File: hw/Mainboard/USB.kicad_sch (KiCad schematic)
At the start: 10 parts, among them J14 USB2.0_HOST_TYPE_C, J8 BOOTSEL

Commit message: wip
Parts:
- removed J8: BOOTSEL, Connector_PinHeader_2.54mm:PinHeader_1x04_P2.54mm_Vertical, symbol Connector:Conn_01x04_Male
- removed R73, R74: 5k1, Resistor_SMD:R_0402_1005Metric, symbol Device:R_Small
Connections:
- net +5V: now also PT19.1, PT20.1
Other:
- note added: "USB 2.0 Host over USB-C connector The 56k pullups on CC1 and CC2 identify as a downstream facing port supplying up to 900ma @ 5V."
- note removed: "USB 2.0 Host over USB-C connector As a host, the 56k pullups on CC1 and CC2 identify USB-C as a power source supplying up to 900ma @ 5V. When flashing the MCU, the 5.1k pulldowns on CC1 and CC2 identify USB-C as a power consumer."
- moved on the sheet: R35, R36

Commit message: hw: routing / silk wip
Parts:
- added C84: 10u, Capacitor_SMD:C_0603_1608Metric, symbol Device:C_Small
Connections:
- net +5V: now also C84.1
- net PD_GND: now also C84.2
- net VBUS1: now reaches J14.A4_B9 (VBUS), PT19.2, R35.1
- net VBUS2: now reaches J14.A9_B4 (VBUS), PT20.2, R36.1
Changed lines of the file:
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@@
   (junction (at 122.555 77.47) (diameter 0) (color 0 0 0 0)
+  )
+  (junction (at 102.87 77.47) (diameter 0) (color 0 0 0 0)
   )
   (no_connect (at 137.16 105.41))
   (no_connect (at 137.16 107.95))
   (wire (pts (xy 137.16 95.25) (xy 135.89 95.25))
+    (stroke (width 0) (type default) (color 0 0 0 0))
+  )
+  (wire (pts (xy 102.87 86.36) (xy 102.87 88.9))
     (stroke (width 0) (type default) (color 0 0 0 0))
   )
@@
     (stroke (width 0) (type default) (color 0 0 0 0))
   )
+  (wire (pts (xy 102.87 77.47) (xy 102.87 81.28))
+    (stroke (width 0) (type default) (color 0 0 0 0))
+  )
   (wire (pts (xy 125.73 85.09) (xy 122.555 85.09))
     (stroke (width 0) (type default) (color 0 0 0 0))
@@
     (effects (font (size 1.27 1.27)) (justify left bottom))
   )
+  (label "VBUS2" (at 129.54 77.47 0)
+    (effects (font (size 1.27 1.27)) (justify left bottom))
+  )
   (label "CC2" (at 137.16 85.09 180)
     (effects (font (size 1.27 1.27)) (justify right bottom))
+  )
+  (label "VBUS1" (at 129.54 74.93 0)
+    (effects (font (size 1.27 1.27)) (justify left bottom))
   )
   (label "CC1" (at 137.16 82.55 180)
@@
     (effects (font (size 1.27 1.27)) (justify right))
   )
+  (symbol (lib_id "Device:C_Small") (at 102.87 83.82 0) (unit 1)
+    (in_bom yes) (on_board yes)
+    (property "Reference" "C84" (id 0) (at 105.2068 82.6516 0)
+      (effects (font (size 1.27 1.27)) (justify left))
+    )
+    (property "Value" "10u" (id 1) (at 105.2068 84.963 0)
+      (effects (font (size 1.27 1.27)) (justify left))
+    )
+    (property "Footprint" "Capacitor_SMD:C_0603_1608Metric" (id 2) (at 102.87 83.82 0)
+      (effects (font (size 1.27 1.27)) hide)
+    )
+    (property "Datasheet" "https://datasheet.lcsc.com/lcsc/2304140030_Samsung-Electro-Mechanics-CL10A106MA8NRNC_C96446.pdf" (id 3) (at 102.87 83.82 0)
+      (effects (font (size 1.27 1.27)) hide)
+    )
+    (property "LCSC" "C96446" (id 4) (at 102.87 83.82 0)
+      (effects (font (size 1.27 1.27)) hide)
+    )
+    (pin "1")
+    (pin "2")
+  )
+  (symbol (lib_id "PET:PD_GND") (at 102.87 88.9 0) (unit 1)
+    (in_bom yes) (on_board yes) (fields_autoplaced)
+    (property "Reference" "#PWR0206" (id 0) (at 102.87 95.25 0)
+      (effects (font (size 1.27 1.27)) hide)
+    )
+    (property "Value" "PD_GND" (id 1) (at 102.87 93.98 0))
+    (property "Footprint" "" (id 2) (at 102.87 88.9 0)
+      (effects (font (size 1.27 1.27)) hide)
+    )
+    (property "Datasheet" "" (id 3) (at 102.87 88.9 0)
+      (effects (font (size 1.27 1.27)) hide)
+    )
+    (pin "1")
+  )
   (symbol (lib_id "PET:PowerTie_2") (at 113.03 74.93 0) (unit 1)

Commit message: hw: unstitched copper fills
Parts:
- C84: value 10u -> 4.7u 16V; LCSC C96446 -> C19666
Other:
- note added: "USB 2.0 Host over USB-C connector The 56k pullups on CC1 and CC2 identify as a downstream facing port supplying 5V @ 900ma."
- note removed: "USB 2.0 Host over USB-C connector The 56k pullups on CC1 and CC2 identify as a downstream facing port supplying up to 900ma @ 5V."
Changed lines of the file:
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@@
     (stroke (width 0) (type default) (color 0 0 0 0))
   )
-  (text "USB 2.0 Host over USB-C connector\n\nThe 56k pullups on CC1 and CC2 identify as a downstream\nfacing port supplying up to 900ma @ 5V."
-    (at 80.01 123.19 0)
+  (text "USB 2.0 Host over USB-C connector\n\nThe 56k pullups on CC1 and CC2 identify as a\ndownstream facing port supplying 5V @ 900ma."
+    (at 83.82 114.3 0)
     (effects (font (size 1.27 1.27)) (justify left bottom))
   )
@@
       (effects (font (size 1.27 1.27)) (justify left))
     )
-    (property "Value" "10u" (id 1) (at 105.2068 84.963 0)
+    (property "Value" "4.7u 16V" (id 1) (at 105.2068 84.963 0)
       (effects (font (size 1.27 1.27)) (justify left))
     )
@@
       (effects (font (size 1.27 1.27)) hide)
     )
-    (property "Datasheet" "https://datasheet.lcsc.com/lcsc/2304140030_Samsung-Electro-Mechanics-CL10A106MA8NRNC_C96446.pdf" (id 3) (at 102.87 83.82 0)
+    (property "Datasheet" "" (id 3) (at 102.87 83.82 0)
       (effects (font (size 1.27 1.27)) hide)
     )
-    (property "LCSC" "C96446" (id 4) (at 102.87 83.82 0)
+    (property "LCSC" "C19666" (id 4) (at 102.87 83.82 0)
       (effects (font (size 1.27 1.27)) hide)
     )

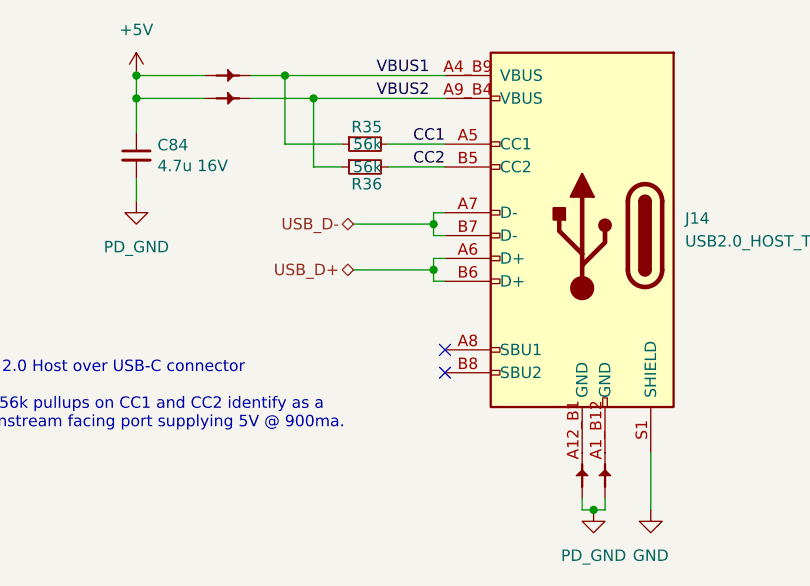
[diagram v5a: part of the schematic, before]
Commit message: hw: heat sink, trace size, more stitching
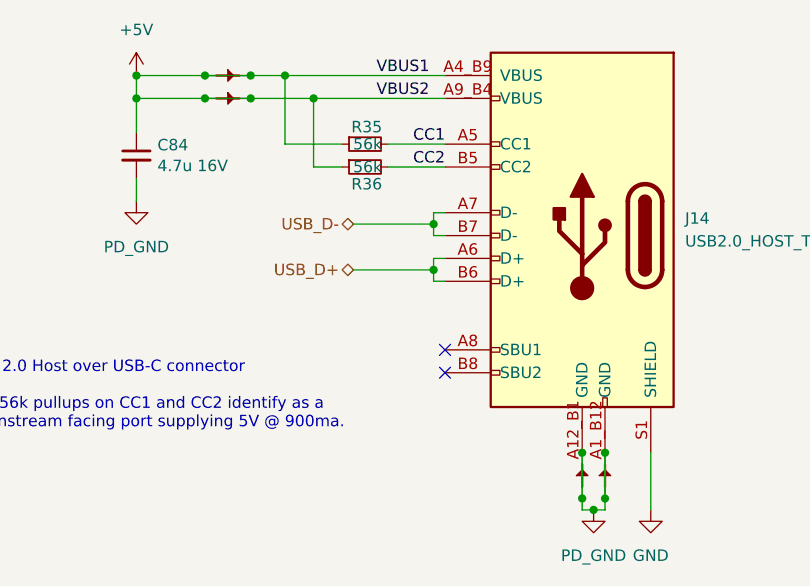
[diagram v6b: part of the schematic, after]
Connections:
- net VBUS1 is gone; now on net +5V: J14.A4_B9 (VBUS), PT19.2, R35.1
- net VBUS2 is gone; now on net +5V: J14.A9_B4 (VBUS), PT20.2, R36.1
- net PD_GND: now also J14.A12_B1 (GND), J14.A1_B12 (GND), PT10.2, PT11.2
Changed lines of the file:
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@@
     (title "CBM PET Mainboard Replacement")
   )
+  (junction (at 110.49 74.93) (diameter 0) (color 0 0 0 0)
+  )
   (junction (at 153.67 123.19) (diameter 0) (color 0 0 0 0)
+  )
+  (junction (at 115.57 74.93) (diameter 0) (color 0 0 0 0)
   )
   (junction (at 102.87 74.93) (diameter 0) (color 0 0 0 0)
@@
   (junction (at 119.38 74.93) (diameter 0) (color 0 0 0 0)
   )
+  (junction (at 152.4 121.92) (diameter 0) (color 0 0 0 0)
+  )
   (junction (at 135.89 91.44) (diameter 0) (color 0 0 0 0)
+  )
+  (junction (at 154.94 116.84) (diameter 0) (color 0 0 0 0)
   )
   (junction (at 122.555 77.47) (diameter 0) (color 0 0 0 0)
   )
+  (junction (at 115.57 77.47) (diameter 0) (color 0 0 0 0)
+  )
+  (junction (at 152.4 116.84) (diameter 0) (color 0 0 0 0)
+  )
+  (junction (at 110.49 77.47) (diameter 0) (color 0 0 0 0)
+  )
   (junction (at 102.87 77.47) (diameter 0) (color 0 0 0 0)
+  )
+  (junction (at 154.94 121.92) (diameter 0) (color 0 0 0 0)
   )
   (no_connect (at 137.16 105.41))
   (no_connect (at 137.16 107.95))
   (wire (pts (xy 137.16 95.25) (xy 135.89 95.25))
+    (stroke (width 0) (type default) (color 0 0 0 0))
+  )
+  (wire (pts (xy 154.94 116.84) (xy 154.94 121.92))
     (stroke (width 0) (type default) (color 0 0 0 0))
   )
@@
   )
   (wire (pts (xy 102.87 74.93) (xy 110.49 74.93))
+    (stroke (width 0) (type default) (color 0 0 0 0))
+  )
+  (wire (pts (xy 110.49 77.47) (xy 115.57 77.47))
     (stroke (width 0) (type default) (color 0 0 0 0))
   )
@@
   )
   (wire (pts (xy 115.57 77.47) (xy 122.555 77.47))
+    (stroke (width 0) (type default) (color 0 0 0 0))
+  )
+  (wire (pts (xy 152.4 116.84) (xy 152.4 121.92))
     (stroke (width 0) (type default) (color 0 0 0 0))
   )
@@
     (stroke (width 0) (type default) (color 0 0 0 0))
   )
+  (wire (pts (xy 110.49 74.93) (xy 115.57 74.93))
+    (stroke (width 0) (type default) (color 0 0 0 0))
+  )

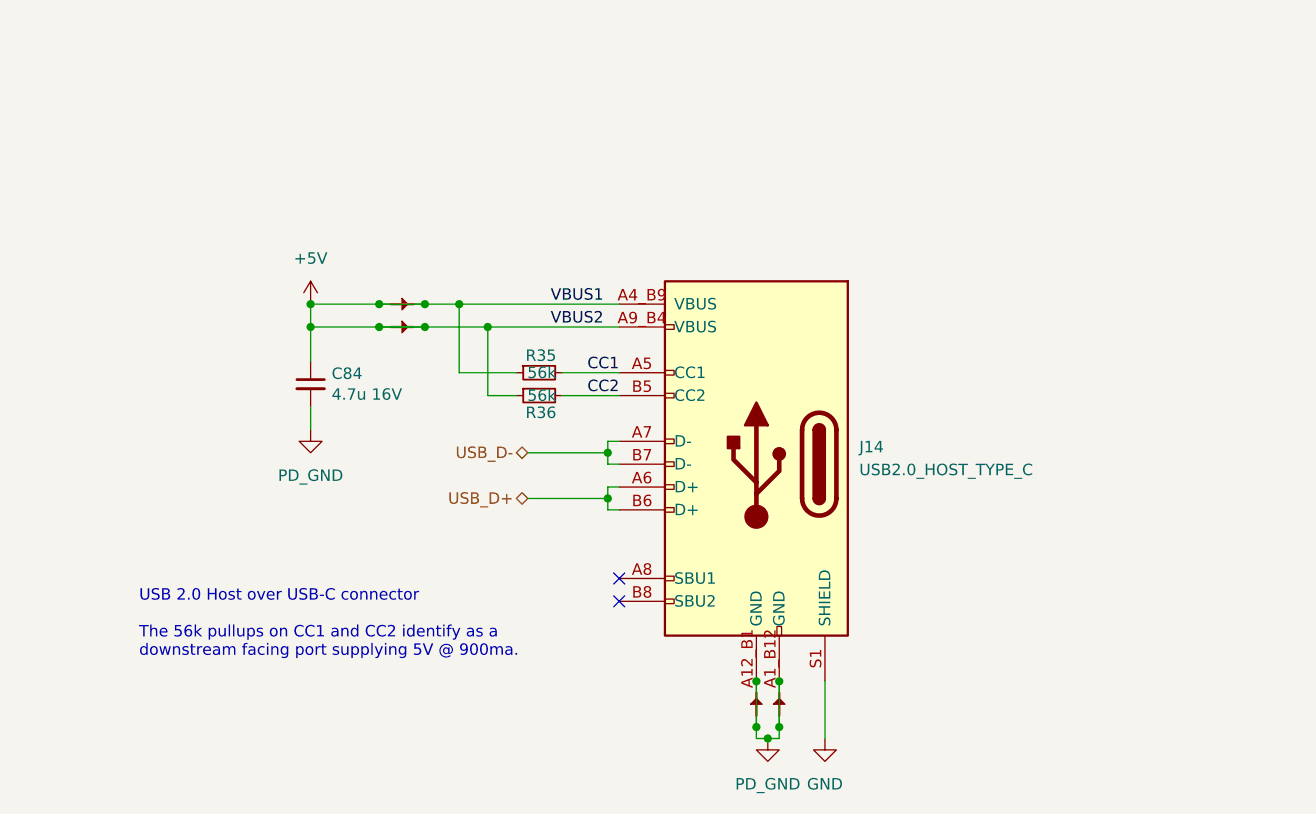
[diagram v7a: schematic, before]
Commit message: hw: 9V DC plug on left edge, change default track size
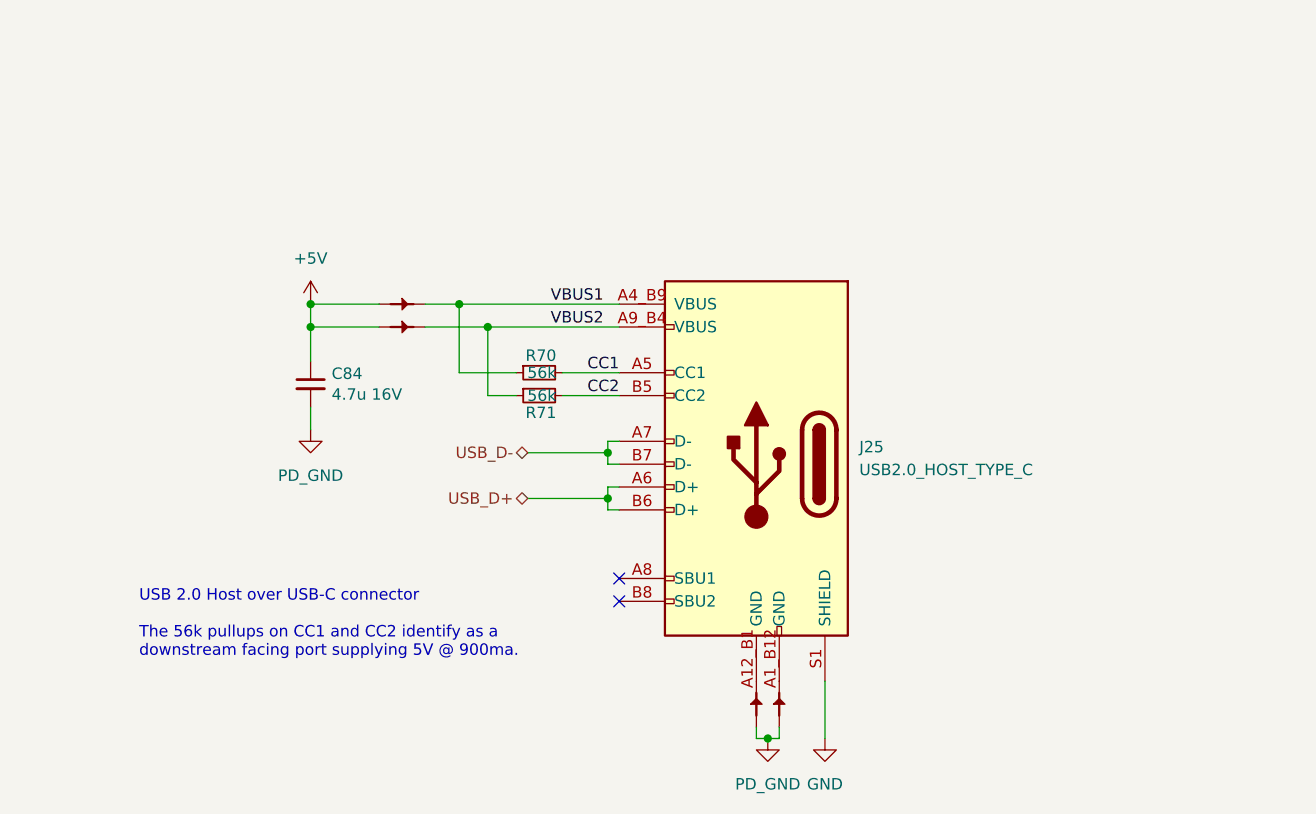
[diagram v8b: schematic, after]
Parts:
- renumbered J14 to J25, PT19 to PT51, PT20 to PT52, PT10 to PT53, PT11 to PT54, R35 to R70, R36 to R71
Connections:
- net +5V: no longer J25.A4_B9 (VBUS), J25.A9_B4 (VBUS), PT51.2, PT52.2, R70.1, R71.1
- net PD_GND: no longer J25.A12_B1 (GND), J25.A1_B12 (GND), PT53.2, PT54.2
- new net: J25.A12_B1 (GND), PT53.2
- new net: J25.A1_B12 (GND), PT54.2
- new net VBUS1: J25.A4_B9 (VBUS), PT51.2, R70.1
- new net VBUS2: J25.A9_B4 (VBUS), PT52.2, R71.1
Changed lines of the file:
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@@
     (title "CBM PET Mainboard Replacement")
   )
-  (junction (at 110.49 74.93) (diameter 0) (color 0 0 0 0)
-  )
   (junction (at 153.67 123.19) (diameter 0) (color 0 0 0 0)
   )
-  (junction (at 115.57 74.93) (diameter 0) (color 0 0 0 0)
-  )
   (junction (at 102.87 74.93) (diameter 0) (color 0 0 0 0)
   )
@@
   (junction (at 119.38 74.93) (diameter 0) (color 0 0 0 0)
   )
-  (junction (at 152.4 121.92) (diameter 0) (color 0 0 0 0)
-  )
   (junction (at 135.89 91.44) (diameter 0) (color 0 0 0 0)
   )
-  (junction (at 154.94 116.84) (diameter 0) (color 0 0 0 0)
-  )
   (junction (at 122.555 77.47) (diameter 0) (color 0 0 0 0)
   )
-  (junction (at 115.57 77.47) (diameter 0) (color 0 0 0 0)
-  )
-  (junction (at 152.4 116.84) (diameter 0) (color 0 0 0 0)
-  )
-  (junction (at 110.49 77.47) (diameter 0) (color 0 0 0 0)
-  )
   (junction (at 102.87 77.47) (diameter 0) (color 0 0 0 0)
-  )
-  (junction (at 154.94 121.92) (diameter 0) (color 0 0 0 0)
   )
   (no_connect (at 137.16 105.41))
@@
     (stroke (width 0) (type default) (color 0 0 0 0))
   )
-  (wire (pts (xy 154.94 116.84) (xy 154.94 121.92))
-    (stroke (width 0) (type default) (color 0 0 0 0))
-  )
   (wire (pts (xy 102.87 86.36) (xy 102.87 88.9))
     (stroke (width 0) (type default) (color 0 0 0 0))
@@
     (stroke (width 0) (type default) (color 0 0 0 0))
   )
-  (wire (pts (xy 110.49 77.47) (xy 115.57 77.47))
-    (stroke (width 0) (type default) (color 0 0 0 0))
-  )
   (wire (pts (xy 122.555 77.47) (xy 137.16 77.47))
     (stroke (width 0) (type default) (color 0 0 0 0))
@@
     (stroke (width 0) (type default) (color 0 0 0 0))
   )
-  (wire (pts (xy 152.4 116.84) (xy 152.4 121.92))
-    (stroke (width 0) (type default) (color 0 0 0 0))
-  )
   (wire (pts (xy 119.38 74.93) (xy 137.16 74.93))
     (stroke (width 0) (type default) (color 0 0 0 0))
@@
   )
   (wire (pts (xy 135.89 90.17) (xy 135.89 91.44))
-    (stroke (width 0) (type default) (color 0 0 0 0))
-  )
-  (wire (pts (xy 110.49 74.93) (xy 115.57 74.93))
     (stroke (width 0) (type default) (color 0 0 0 0))
   )
@@
   (symbol (lib_id "PET:PD_GND") (at 102.87 88.9 0) (unit 1)
     (in_bom yes) (on_board yes) (fields_autoplaced)
-    (property "Reference" "#PWR0206" (id 0) (at 102.87 95.25 0)
+    (property "Reference" "#PWR0150" (id 0) (at 102.87 95.25 0)
       (effects (font (size 1.27 1.27)) hide)
     )
@@
   (symbol (lib_id "PET:PowerTie_2") (at 113.03 74.93 0) (unit 1)
     (in_bom yes) (on_board yes) (fields_autoplaced)
-    (property "Reference" "PT19" (id 0) (at 113.03 73.025 0)
+    (property "Reference" "PT51" (id 0) (at 113.03 73.025 0)
       (effects (font (size 1.27 1.27)) hide)
     )
@@
   (symbol (lib_id "JLCPCB:USB_C_Receptacle_USB2.0") (at 152.4 92.71 0) (mirror y) (unit 1)
     (in_bom yes) (on_board yes) (fields_autoplaced)
-    (property "Reference" "J14" (id 0) (at 163.83 90.8049 0)
+    (property "Reference" "J25" (id 0) (at 163.83 90.8049 0)
       (effects (font (size 1.27 1.27)) (justify right))
     )
@@
   (symbol (lib_id "PET:PowerTie_2") (at 154.94 119.38 90) (unit 1)
     (in_bom yes) (on_board yes) (fields_autoplaced)
-    (property "Reference" "PT11" (id 0) (at 153.035 119.38 0)
+    (property "Reference" "PT54" (id 0) (at 153.035 119.38 0)
       (effects (font (size 1.27 1.27)) hide)
     )
@@
   (symbol (lib_id "Device:R_Small") (at 128.27 85.09 90) (mirror x) (unit 1)
     (in_bom yes) (on_board yes)
-    (property "Reference" "R36" (id 0) (at 130.175 86.995 90)
+    (property "Reference" "R71" (id 0) (at 130.175 86.995 90)
       (effects (font (size 1.27 1.27)) (justify left))
     )
@@
   (symbol (lib_id "PET:PowerTie_2") (at 152.4 119.38 90) (unit 1)
     (in_bom yes) (on_board yes) (fields_autoplaced)
-    (property "Reference" "PT10" (id 0) (at 150.495 119.38 0)
+    (property "Reference" "PT53" (id 0) (at 150.495 119.38 0)
       (effects (font (size 1.27 1.27)) hide)
     )
@@
   (symbol (lib_id "power:+5V") (at 102.87 74.93 0) (mirror y) (unit 1)
     (in_bom yes) (on_board yes) (fields_autoplaced)
-    (property "Reference" "#PWR045" (id 0) (at 102.87 78.74 0)
+    (property "Reference" "#PWR0149" (id 0) (at 102.87 78.74 0)
       (effects (font (size 1.27 1.27)) hide)
     )
@@
   (symbol (lib_id "Device:R_Small") (at 128.27 82.55 90) (mirror x) (unit 1)
     (in_bom yes) (on_board yes)
-    (property "Reference" "R35" (id 0) (at 130.175 80.645 90)
+    (property "Reference" "R70" (id 0) (at 130.175 80.645 90)
       (effects (font (size 1.27 1.27)) (justify left))
     )
@@
   (symbol (lib_id "PET:PD_GND") (at 153.67 123.19 0) (unit 1)
     (in_bom yes) (on_board yes) (fields_autoplaced)
-    (property "Reference" "#PWR0164" (id 0) (at 153.67 129.54 0)
+    (property "Reference" "#PWR0151" (id 0) (at 153.67 129.54 0)
       (effects (font (size 1.27 1.27)) hide)
     )
@@
   (symbol (lib_id "PET:PowerTie_2") (at 113.03 77.47 0) (unit 1)
     (in_bom yes) (on_board yes) (fields_autoplaced)
-    (property "Reference" "PT20" (id 0) (at 113.03 75.565 0)
+    (property "Reference" "PT52" (id 0) (at 113.03 75.565 0)
       (effects (font (size 1.27 1.27)) hide)
     )
@@
   (symbol (lib_id "power:GND") (at 160.02 123.19 0) (unit 1)
     (in_bom yes) (on_board yes) (fields_autoplaced)
-    (property "Reference" "#PWR0165" (id 0) (at 160.02 129.54 0)
-      (effects (font (size 1.27 1.27)) hide)
-    )
+    (property "Reference" "#PWR0152" (id 0) (at 160.02 129.54 0)
+      (effects (font (size 1.27 1.27)) hide)
+    )
